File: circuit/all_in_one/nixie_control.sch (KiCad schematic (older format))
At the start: 19 parts, among them IC1 ATMEGA328P-A, P2 CONN_02X04, SW1 SW_PUSH, SW2 SW_PUSH, U3 TLP521, U4 TLP521, U5 HEF4028, U6 K155ID1, U7 TLP521, U8 TLP521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

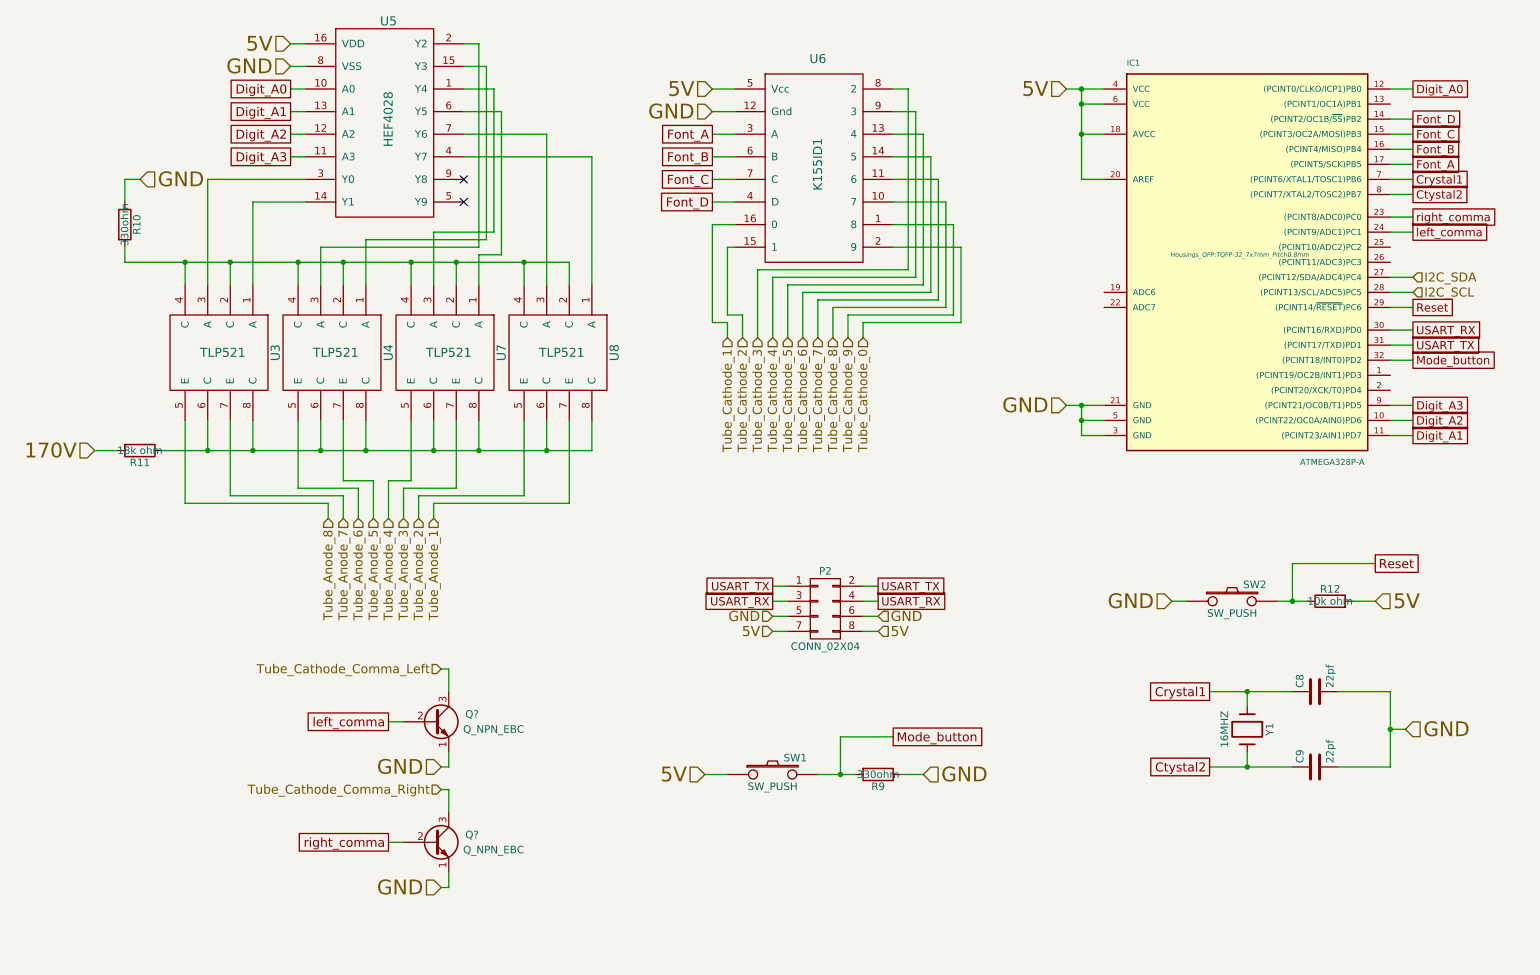
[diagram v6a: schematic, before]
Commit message: [All in one]Select resister and power jack's footprint
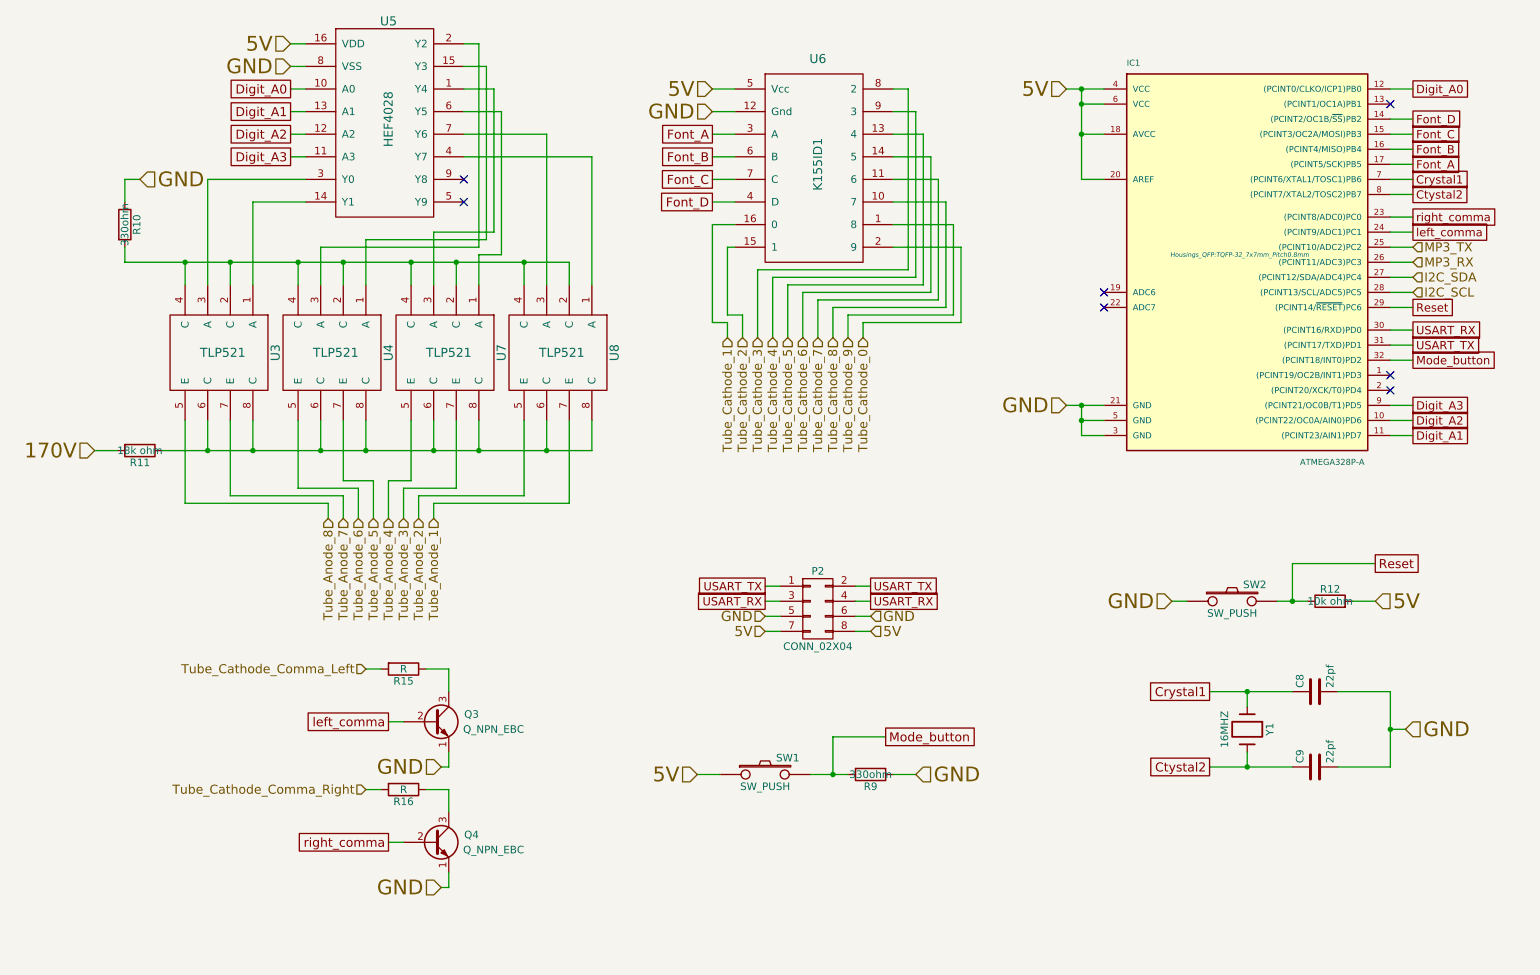
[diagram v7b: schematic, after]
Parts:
- added R15, R16: R, Resistors_SMD:R_0805_HandSoldering, symbol R
- P2: footprint (none) -> Socket_Strips:Socket_Strip_Straight_2x04
- Q3, Q4: renamed from Q?; footprint (none) -> Housings_TO-92:TO-92_Inline_Narrow_Oval
- R10, R11, R12, R9: footprint (none) -> Resistors_SMD:R_0805_HandSoldering
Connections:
- net Tube_Cathode_Comma_Left: now also R15.2; no longer Q3.3 (C)
- net Tube_Cathode_Comma_Right: now also R16.2; no longer Q4.3 (C)
- net MP3_TX: now reaches IC1.25 ((PCINT10/ADC2)PC2)
- net MP3_RX: now reaches IC1.26 ((PCINT11/ADC3)PC3)
- new net: Q3.3 (C), R15.1
- new net: Q4.3 (C), R16.1
- no-connect marks 2 -> 7
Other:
- moved on the sheet: P2, R9, SW1
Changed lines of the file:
@@
 F 0 "R12" V 9530 4850 50  0000 C CNN
 F 1 "10k ohm" V 9450 4850 50  0000 C CNN
-F 2 "" V 9380 4850 30  0001 C CNN
+F 2 "Resistors_SMD:R_0805_HandSoldering" V 9380 4850 30  0001 C CNN
 F 3 "" H 9450 4850 30  0000 C CNN
 	1    9450 4850
@@
 F 0 "R11" V 1630 3850 50  0000 C CNN
 F 1 "18k ohm" V 1550 3850 50  0000 C CNN
-F 2 "" V 1480 3850 30  0001 C CNN
+F 2 "Resistors_SMD:R_0805_HandSoldering" V 1480 3850 30  0001 C CNN
 F 3 "" H 1550 3850 30  0000 C CNN
 	1    1550 3850
@@
 L CONN_02X04 P2
 U 1 1 56476352
-P 6100 4900
-F 0 "P2" H 6100 5150 50  0000 C CNN
-F 1 "CONN_02X04" H 6100 4650 50  0000 C CNN
-F 2 "" H 6100 3700 60  0001 C CNN
-F 3 "" H 6100 3700 60  0000 C CNN
-	1    6100 4900
+P 6050 4900
+F 0 "P2" H 6050 5150 50  0000 C CNN
+F 1 "CONN_02X04" H 6050 4650 50  0000 C CNN
+F 2 "Socket_Strips:Socket_Strip_Straight_2x04" H 6050 3700 60  0001 C CNN
+F 3 "" H 6050 3700 60  0000 C CNN
+	1    6050 4900
 	1    0    0    -1
 $EndComp
-Text HLabel 5750 5050 0    67   Input ~ 0
+Text HLabel 5700 5050 0    67   Input ~ 0
 5V
-Text HLabel 5750 4950 0    67   Input ~ 0
-GND
-Wire Wire Line
-	5750 4950 5850 4950
-Text HLabel 6450 5050 2    67   Input ~ 0
+Text HLabel 5700 4950 0    67   Input ~ 0
+GND
+Wire Wire Line
+	5700 4950 5800 4950
+Text HLabel 6400 5050 2    67   Input ~ 0
 5V
-Text HLabel 6450 4950 2    67   Input ~ 0
-GND
-Wire Wire Line
-	6350 4950 6450 4950
-Text GLabel 5750 4850 0    55   UnSpc ~ 0
+Text HLabel 6400 4950 2    67   Input ~ 0
+GND
+Wire Wire Line
+	6300 4950 6400 4950
+Text GLabel 5700 4850 0    55   UnSpc ~ 0
 USART_RX
-Text GLabel 5750 4750 0    55   UnSpc ~ 0
+Text GLabel 5700 4750 0    55   UnSpc ~ 0
 USART_TX
-Text GLabel 6450 4850 2    55   UnSpc ~ 0
+Text GLabel 6400 4850 2    55   UnSpc ~ 0
 USART_RX
-Text GLabel 6450 4750 2    55   UnSpc ~ 0
+Text GLabel 6400 4750 2    55   UnSpc ~ 0
 USART_TX
 Wire Wire Line
-	5750 4750 5850 4750
-Wire Wire Line
-	5750 4850 5850 4850
-Wire Wire Line
-	6350 4750 6450 4750
-Wire Wire Line
-	6450 4850 6350 4850
-Wire Wire Line
-	6450 5050 6350 5050
-Wire Wire Line
-	5750 5050 5850 5050
+	5700 4750 5800 4750
+Wire Wire Line
+	5700 4850 5800 4850
+Wire Wire Line
+	6300 4750 6400 4750
+Wire Wire Line
+	6400 4850 6300 4850
+Wire Wire Line
+	6400 5050 6300 5050
+Wire Wire Line
+	5700 5050 5800 5050
 Text GLabel 10000 3250 2    55   UnSpc ~ 0
 Mode_button
 Wire Wire Line
 	10000 3250 9850 3250
-Text HLabel 5300 6000 0    98   Input ~ 0
+Text HLabel 5250 6000 0    98   Input ~ 0
 5V
 $Comp
 L SW_PUSH SW1
 U 1 1 56478717
-P 5750 6000
-F 0 "SW1" H 5900 6110 50  0000 C CNN
-F 1 "SW_PUSH" H 5750 5920 50  0000 C CNN
-F 2 "" H 5750 6000 60  0001 C CNN
-F 3 "" H 5750 6000 60  0000 C CNN
-	1    5750 6000
+P 5700 6000
+F 0 "SW1" H 5850 6110 50  0000 C CNN
+F 1 "SW_PUSH" H 5700 5920 50  0000 C CNN
+F 2 "" H 5700 6000 60  0001 C CNN
+F 3 "" H 5700 6000 60  0000 C CNN
+	1    5700 6000
 	1    0    0    -1
 $EndComp
@@
 L R R9
 U 1 1 5647877C
-P 6450 6000
-F 0 "R9" V 6530 6000 50  0000 C CNN
-F 1 "330ohm" V 6450 6000 50  0000 C CNN
-F 2 "" V 6380 6000 30  0001 C CNN
-F 3 "" H 6450 6000 30  0000 C CNN
-	1    6450 6000
-	0    1    1    0
-$EndComp
-Text HLabel 6750 6000 2    98   Input ~ 0
-GND
-Wire Wire Line
-	6600 6000 6750 6000
-Wire Wire Line
-	6050 6000 6300 6000
-Wire Wire Line
-	5300 6000 5450 6000
-Text GLabel 6550 5750 2    60   UnSpc ~ 0
+P 6400 6000
+F 0 "R9" V 6480 6000 50  0000 C CNN
+F 1 "330ohm" V 6400 6000 50  0000 C CNN
+F 2 "Resistors_SMD:R_0805_HandSoldering" V 6330 6000 30  0001 C CNN
+F 3 "" H 6400 6000 30  0000 C CNN
+	1    6400 6000
+	0    1    1    0
+$EndComp
+Text HLabel 6700 6000 2    98   Input ~ 0
+GND
+Wire Wire Line
+	6550 6000 6700 6000
+Wire Wire Line
+	6000 6000 6250 6000
+Wire Wire Line
+	5250 6000 5400 6000
+Text GLabel 6500 5750 2    60   UnSpc ~ 0
 Mode_button
 Wire Wire Line
-	6200 6000 6200 5750
-Wire Wire Line
-	6200 5750 6550 5750
-Connection ~ 6200 6000
+	6150 6000 6150 5750
+Wire Wire Line
+	6150 5750 6500 5750
+Connection ~ 6150 6000
 $Comp
 L R R10
@@
 F 0 "R10" V 1530 2350 50  0000 C CNN
 F 1 "330ohm" V 1450 2350 50  0000 C CNN
-F 2 "" V 1380 2350 30  0001 C CNN
+F 2 "Resistors_SMD:R_0805_HandSoldering" V 1380 2350 30  0001 C CNN
 F 3 "" H 1450 2350 30  0000 C CNN
 	1    1450 2350
@@
 Tube_Cathode_0
 $Comp
-L Q_NPN_EBC Q?
+L Q_NPN_EBC Q3
 U 1 1 56531503
 P 3500 5650
-F 0 "Q?" H 3800 5700 50  0000 R CNN
+F 0 "Q3" H 3800 5700 50  0000 R CNN
 F 1 "Q_NPN_EBC" H 4100 5600 50  0000 R CNN
-F 2 "" H 3700 5750 29  0000 C CNN
+F 2 "Housings_TO-92:TO-92_Inline_Narrow_Oval" H 3700 5750 29  0001 C CNN
 F 3 "" H 3500 5650 60  0000 C CNN
 	1    3500 5650
@@
 $EndComp
 $Comp
-L Q_NPN_EBC Q?
+L Q_NPN_EBC Q4
 U 1 1 56531680
 P 3500 6450
-F 0 "Q?" H 3800 6500 50  0000 R CNN
+F 0 "Q4" H 3800 6500 50  0000 R CNN
 F 1 "Q_NPN_EBC" H 4100 6400 50  0000 R CNN
-F 2 "" H 3700 6550 29  0000 C CNN
+F 2 "Housings_TO-92:TO-92_Inline_Narrow_Oval" H 3700 6550 29  0001 C CNN
 F 3 "" H 3500 6450 60  0000 C CNN
 	1    3500 6450
 	1    0    0    -1
 $EndComp
-Text HLabel 3550 5300 0    60   Input ~ 0
+Text HLabel 3050 5300 0    60   Input ~ 0
 Tube_Cathode_Comma_Left
-Text HLabel 3550 6100 0    60   Input ~ 0
+Text HLabel 3050 6100 0    60   Input ~ 0
 Tube_Cathode_Comma_Right
 Wire Wire Line
-	3550 5300 3600 5300
+	3450 5300 3600 5300
 Wire Wire Line
 	3600 5300 3600 5450
 Wire Wire Line
-	3550 6100 3600 6100
+	3450 6100 3600 6100
 Wire Wire Line
 	3600 6100 3600 6250
@@
 Wire Wire Line
 	9850 1950 10000 1950
+$Comp
+L R R15
+U 1 1 5656B24C
+P 3300 5300
+F 0 "R15" V 3380 5300 50  0000 C CNN
+F 1 "R" V 3300 5300 50  0000 C CNN
+F 2 "Resistors_SMD:R_0805_HandSoldering" V 3230 5300 30  0001 C CNN
+F 3 "" H 3300 5300 30  0000 C CNN
+	1    3300 5300
+	0    1    1    0
+$EndComp
+Wire Wire Line
+	3050 5300 3150 5300
+$Comp
+L R R16
+U 1 1 5656B5EC
+P 3300 6100
+F 0 "R16" V 3380 6100 50  0000 C CNN
+F 1 "R" V 3300 6100 50  0000 C CNN
+F 2 "Resistors_SMD:R_0805_HandSoldering" V 3230 6100 30  0001 C CNN
+F 3 "" H 3300 6100 30  0000 C CNN
+	1    3300 6100
+	0    1    1    0
+$EndComp
+Wire Wire Line
+	3050 6100 3150 6100
+Text HLabel 10000 2500 2    60   Input ~ 0
+MP3_TX
+Text HLabel 10000 2600 2    60   Input ~ 0
+MP3_RX
+Wire Wire Line
+	9850 2500 10000 2500
+Wire Wire Line
+	10000 2600 9850 2600
+NoConn ~ 9850 3350
+NoConn ~ 9850 3450
+NoConn ~ 7950 2800
+NoConn ~ 7950 2900
+NoConn ~ 9850 1550
 $EndSCHEMATC

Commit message: [All in one]Select footprint for capacitors
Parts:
- C8, C9: footprint (none) -> Capacitors_SMD:C_0805_HandSoldering
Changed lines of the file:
@@
 F 0 "C8" H 9375 5550 50  0000 L CNN
 F 1 "22pf" H 9375 5350 50  0000 L CNN
-F 2 "" H 9388 5300 30  0001 C CNN
+F 2 "Capacitors_SMD:C_0805_HandSoldering" H 9388 5300 30  0001 C CNN
 F 3 "" H 9350 5450 60  0000 C CNN
 	1    9350 5450
@@
 F 0 "C9" H 9375 6050 50  0000 L CNN
 F 1 "22pf" H 9375 5850 50  0000 L CNN
-F 2 "" H 9388 5800 30  0001 C CNN
+F 2 "Capacitors_SMD:C_0805_HandSoldering" H 9388 5800 30  0001 C CNN
 F 3 "" H 9350 5950 60  0000 C CNN
 	1    9350 5950
